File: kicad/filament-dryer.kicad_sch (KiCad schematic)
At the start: 45 parts, among them J1 Heater, J2 HEATER TEMP, J3 AREF_SELECT, J4 BOX TEMP, J5 Vdd 24V, J6 AVR-ISP-6, J7 Conn_02x07_Odd_Even, Q1 STP75NF75, Q2 2N5401, Q3 2N5551, SW1 SW_Push, U1 MIC4680-5BM, U2 ATmega8-16P, U3 LM336Z-2.5, Y1 10MHz

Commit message: schematic done, ready for pcb layout
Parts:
- removed J7: Conn_02x07_Odd_Even, Connector_PinHeader_2.54mm:PinHeader_2x02_P2.54mm_Vertical, symbol Connector_Generic:Conn_02x07_Odd_Even
- removed Q2: 2N5401, Package_TO_SOT_THT:TO-92_Inline, symbol kicad-ezee-symbols:2N5401
- removed Q3: 2N5551, Package_TO_SOT_THT:TO-92_Inline, symbol kicad-ezee-symbols:2N5551
- added CN1: Pololu Mini-LCD, Connector_PinHeader_2.54mm:PinHeader_2x07_P2.54mm_Vertical, symbol kicad-ezee-symbols:Pololu_Mini_Display
- added J7: Conn_01x06, Connector_PinHeader_2.54mm:PinHeader_1x06_P2.54mm_Vertical, symbol Connector_Generic:Conn_01x06
- added Q3: 2N3906, Package_TO_SOT_THT:TO-92_Inline, symbol Transistor_BJT:2N3906
- added Q4: 2N3904, Package_TO_SOT_THT:TO-92_Inline, symbol Transistor_BJT:2N3904
- added RV1: 10k, kicad-ezee-footprints:Potentiometer_P5.1mm_Vertical, symbol Device:R_Potentiometer_Small
- J1: footprint (none) -> kicad-ezee-footprints:TerminalBlock_2_P5.08mm
- J2, J4: footprint (none) -> Connector_PinHeader_2.54mm:PinHeader_1x02_P2.54mm_Vertical
- J3: footprint (none) -> Connector_PinHeader_2.54mm:PinHeader_2x02_P2.54mm_Vertical
- J5: value Vdd 24V -> Power
- J6: footprint (none) -> Connector_PinHeader_2.54mm:PinHeader_2x03_P2.54mm_Vertical
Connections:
- net +24V: now also C1.1, J5.1 (Pin_1), U1.2 (VIN)
- net +5V: now also C3.1, C4.1, R14.1, U2.7 (VCC), CN1.2 (Vdd), J7.1 (Pin_1), Q3.1 (E), RV1.1
- net GND: now also U1.5 (GND), U1.6 (GND), U1.7 (GND), CN1.1 (Vss), CN1.5 (R/W), J7.6 (Pin_6), Q4.1 (E), RV1.3
- net HEAT_ON: now also U2.14 (PB0)
- net Vgs: now also Q3.3 (C)
- net at R10.1, R8.2: now also Q4.2 (B)
- net at R11.2, R9.1: now also Q4.3 (C)
- net at R11.1: now also Q3.2 (B)
- net LCD_E: now reaches U2.11 (PD5)
- net LCD_E: now also CN1.6 (Enable)
- net LCD_RS: now reaches U2.12 (PD6)
- net LCD_RS: now also CN1.4 (RS)
- net PB1_OC1A: now reaches U2.15 (PB1)
- net PB1_OC1A: now also J7.5 (Pin_5)
- net RX: now reaches U2.2 (PD0)
- net RX: now also J7.2 (Pin_2)
- net LCD_DB4: now reaches U2.25 (PC2)
- net LCD_DB4: now also CN1.11 (DB4)
- net LCD_DB5: now reaches U2.26 (PC3)
- net LCD_DB5: now also CN1.12 (DB5)
- net LCD_DB6: now reaches U2.27 (PC4)
- net LCD_DB6: now also CN1.13 (DB6)
- net LCD_DB7: now reaches U2.28 (PC5)
- net LCD_DB7: now also CN1.14 (DB7)
- net TX: now reaches U2.3 (PD1)
- net TX: now also J7.3 (Pin_3)
- net PD2_INT0: now reaches U2.4 (PD2)
- net PD2_INT0: now also J7.4 (Pin_4)
- new net: CN1.3 (Vo), RV1.2
- no-connect marks 0 -> 8
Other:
- note removed: "Pololu Mini LCD pinout"
- moved on the sheet: J2, J4, R15, R17

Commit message: added fuses and fans, ready for layout
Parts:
- added F2: 5A, kicad-ezee-footprints:FuseHolder_20x5mm, symbol Device:Polyfuse
- added J8: Fresh Air Fan, Connector_PinHeader_2.54mm:PinHeader_1x02_P2.54mm_Vertical, symbol Connector_Generic:Conn_01x02
- added TH1: 10k, Resistor_THT:R_Axial_DIN0207_L6.3mm_D2.5mm_P10.16mm_Horizontal, symbol Device:Thermistor
- added TJ1: 80 deg, Connector_Wire:SolderWire-0.75sqmm_1x02_P7mm_D1.25mm_OD3.5mm, symbol Device:Thermal_Jumper
- J2: footprint Connector_PinHeader_2.54mm:PinHeader_1x02_P2.54mm_Vertical -> Connector_JST:JST_PH_B2B-PH-K_1x02_P2.00mm_Vertical
- J4: value BOX TEMP -> Circulation Fan
- J5: value Power -> 24V
- J7: value Conn_01x06 -> IO
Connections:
- net +24V: now also J4.1 (Pin_1), F2.2; no longer J5.1 (Pin_1)
- net BOX_TEMP: now also TH1.1; no longer J4.1 (Pin_1)
- net GND: now also J8.2 (Pin_2), TH1.2
- net FAN: now reaches U2.6 (PD4)
- net FAN: now also J8.1 (Pin_1)
- new net: J5.1 (Pin_1), TJ1.1 (Pin1)
- new net: F2.1, TJ1.2 (Pin2)
- no-connect marks 8 -> 7
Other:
- note added: "Runs 30 secs every 10th minute"
- note added: "Runs continously to spread heat in box"
- note added: "Tilsvarende som ovenfor, bruker mindre enn 10k resistor for å få bedre nøyaktighet rundt 50-70 grader."
- moved on the sheet: C1, C2, F1, J7, L1, U1

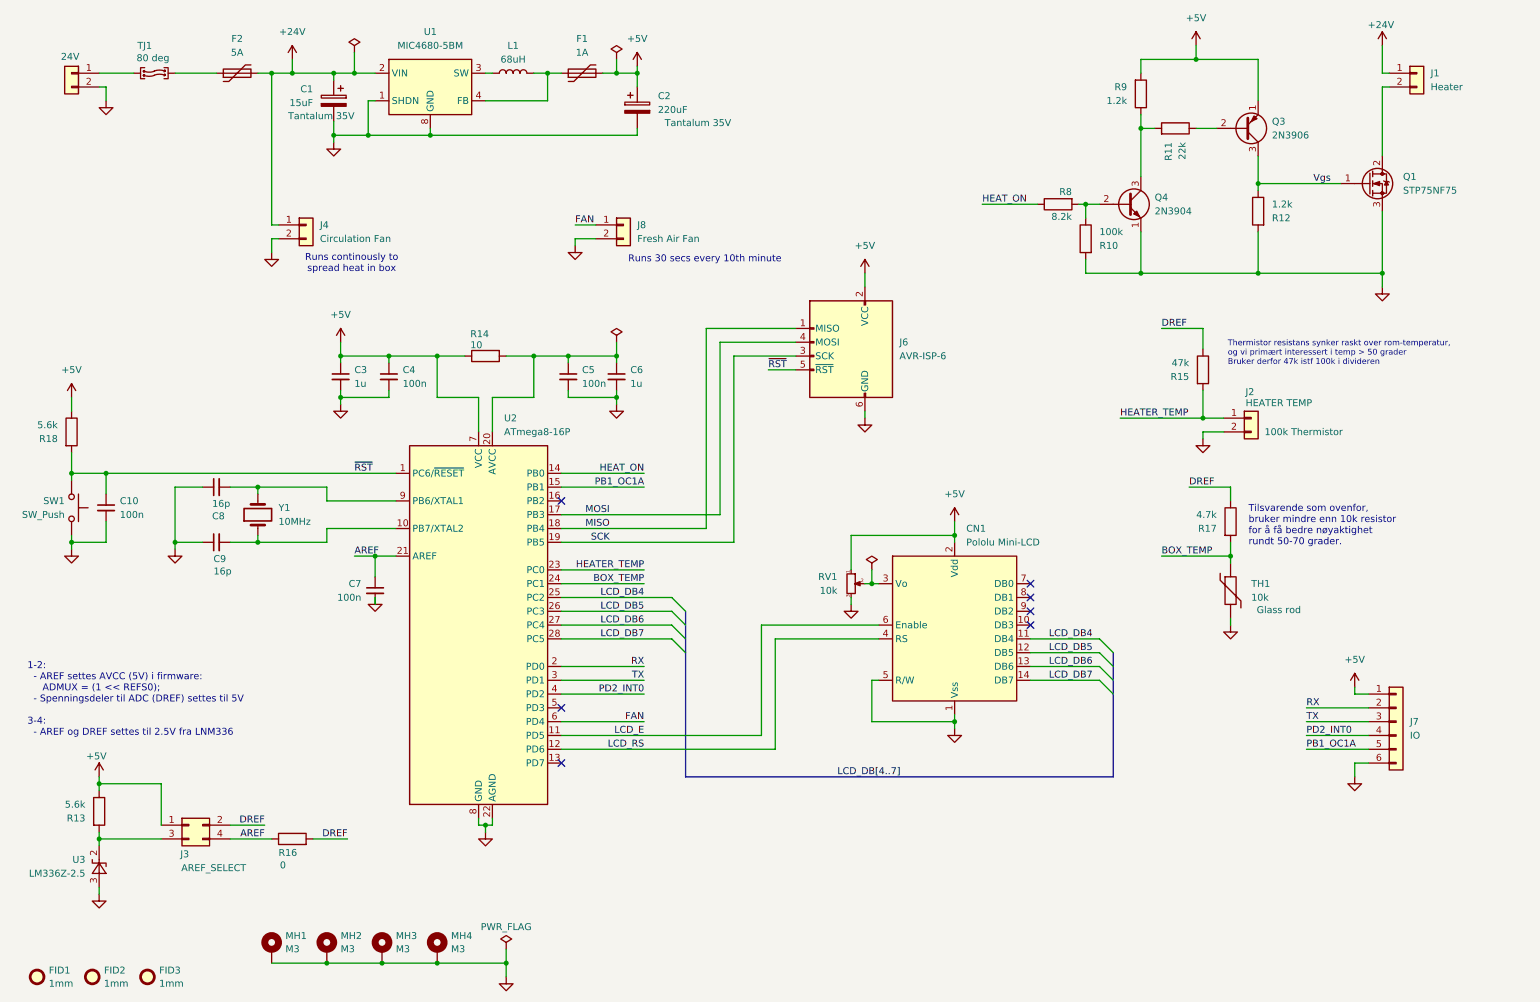
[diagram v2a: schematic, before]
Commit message: fan-control transistor, resistor values in mosfet driver
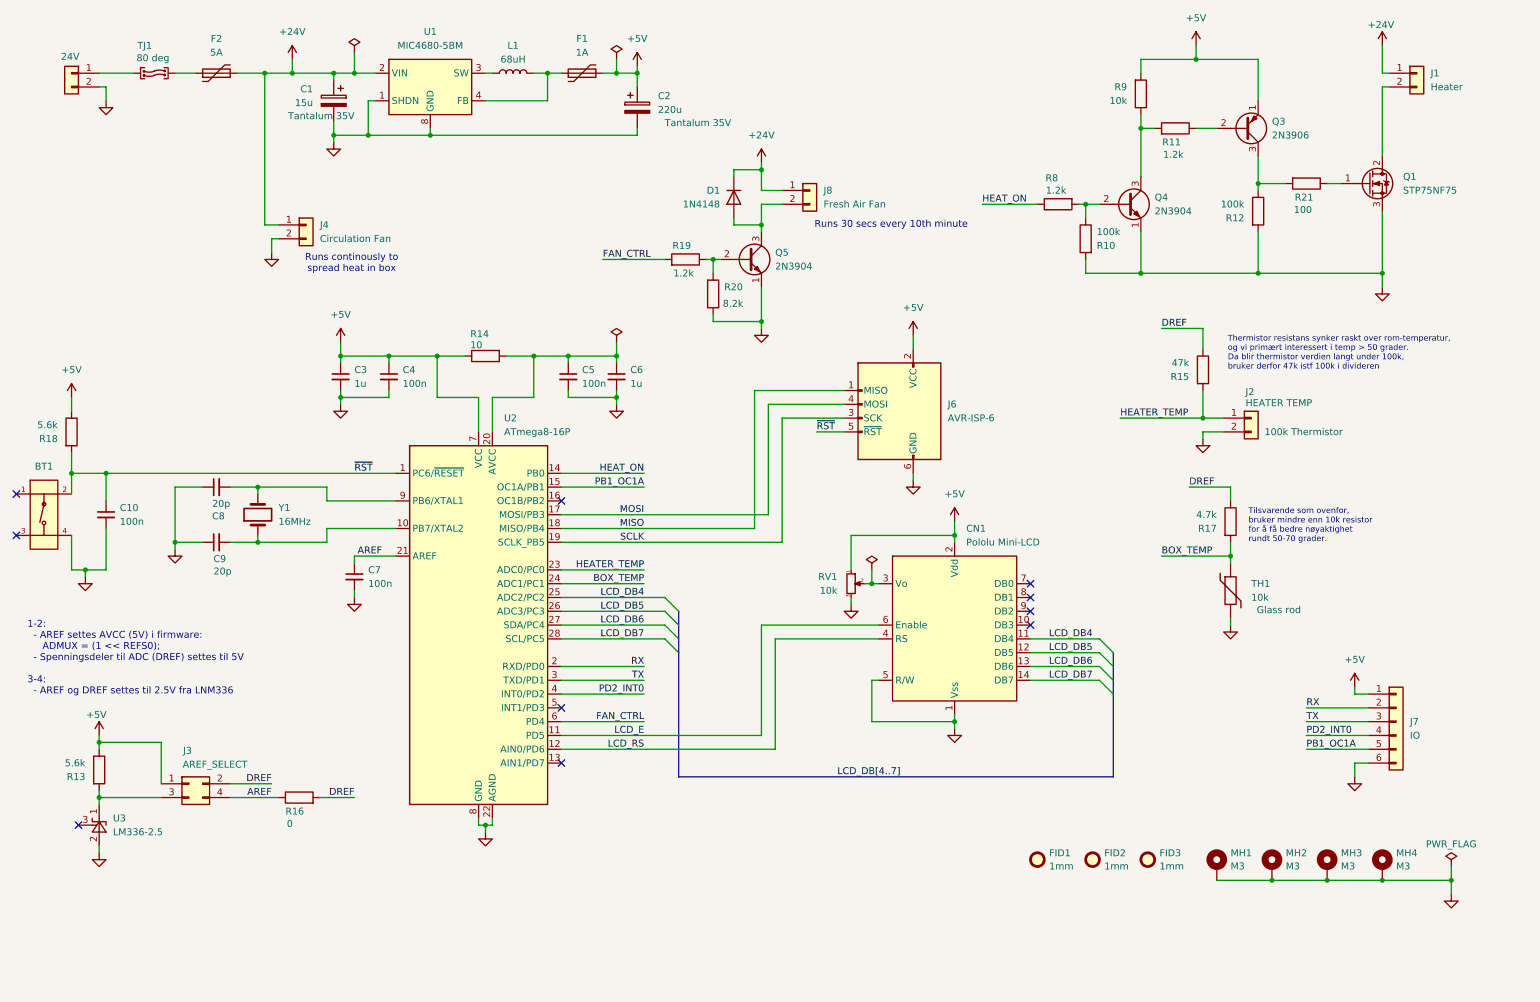
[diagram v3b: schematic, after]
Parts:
- removed SW1: SW_Push, symbol Switch:SW_Push
- removed U3: LM336Z-2.5, Package_TO_SOT_THT:TO-92_Inline, symbol kicad-ezee-symbols:LM336Z-2.5
- added BT1: Tactile Button, kicad-ezee-footprints:PushButton-SMD_4P-L5.1-W5.1, symbol kicad-ezee-symbols:Tactile_Button,_160gf,_12V,_50mA,_5.1mm
- added D1: 1N4148, Diode_THT:D_DO-35_SOD27_P7.62mm_Horizontal, symbol Diode:1N4148
- added Q5: 2N3904, Package_TO_SOT_THT:TO-92_Inline, symbol Transistor_BJT:2N3904
- added R19: 1.2k, Resistor_THT:R_Axial_DIN0207_L6.3mm_D2.5mm_P10.16mm_Horizontal, symbol Device:R
- added R20: 8.2k, Resistor_THT:R_Axial_DIN0207_L6.3mm_D2.5mm_P10.16mm_Horizontal, symbol Device:R
- added R21: 100, Resistor_THT:R_Axial_DIN0207_L6.3mm_D2.5mm_P10.16mm_Horizontal, symbol Device:R
- added U3: LM336-2.5, Package_TO_SOT_THT:TO-92L_Inline, symbol kicad-ezee-symbols:LM336-2.5
- C1: value 15uF -> 15u
- C2: value 220uF -> 220u
- C8, C9: value 16p -> 20p
- R11: value 22k -> 1.2k
- R12: value 1.2k -> 100k
- R8: value 8.2k -> 1.2k
- R9: value 1.2k -> 10k
- RV1: footprint kicad-ezee-footprints:Potentiometer_P5.1mm_Vertical -> kicad-ezee-footprints:Potentiometer_VANXY_T73YP_Vertical
- Y1: value 10MHz -> 16MHz
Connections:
- net +24V: now also J8.1 (Pin_1), D1.1 (K)
- net GND: now also BT1.4 (D), Q5.1 (E), R20.1, U3.2 (A); no longer J8.2 (Pin_2)
- net ~{RST}: now also BT1.2 (B)
- net at J3.3 (Pin_3), R13.2: now also U3.1 (K)
- net FAN renamed FAN_CTRL
- net FAN_CTRL: now also R19.2; no longer J8.1 (Pin_1)
- net SCK renamed SCLK
- net Vgs: no longer names the net of Q3.3 (C), R12.1
- net Vgs: now also R21.2; no longer Q1.1 (G)
- new net: D1.2 (A), J8.2 (Pin_2), Q5.3 (C)
- new net: Q5.2 (B), R19.1, R20.2
- new net: Q1.1 (G), R21.1
- no-connect marks 7 -> 10
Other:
- note added: "Thermistor resistans synker raskt over rom-temperatur, og vi primært interessert i temp > 50 grader. Da blir thermistor verdien langt under 100k, bruker derfor 47k istf 100k i divideren"
- note removed: "Thermistor resistans synker raskt over rom-temperatur, og vi primært interessert i temp > 50 grader Bruker derfor 47k istf 100k i divideren"
- moved on the sheet: C10, C7, F2, FID1, FID2, FID3, J3, J6, J8, MH1, MH2, MH3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

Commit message: Component placement done
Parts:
- C5: renamed from C3; footprint Capacitor_THT:C_Radial_D4.0mm_H5.0mm_P1.50mm -> Capacitor_Tantalum_SMD:CP_EIA-6032-20_AVX-F
- C9: renamed from C6; footprint Capacitor_THT:C_Radial_D4.0mm_H5.0mm_P1.50mm -> Capacitor_Tantalum_SMD:CP_EIA-6032-20_AVX-F
- renumbered C10 to C1, C2 to C10, C8 to C2, C9 to C3, C1 to C4, C7 to C6, C4 to C7, C5 to C8, F2 to F1, F1 to F2, J5 to J1, J3 to J2, J4 to J3, J8 to J4, J6 to J5, J2 to J6, J1 to J8, Q5 to Q1, Q4 to Q2, Q1 to Q4, R18 to R1, R11 to R10, R15 to R11, R17 to R12, R12 to R13, R21 to R14, R13 to R2, R16 to R3, R14 to R4, R19 to R5, R20 to R6, R8 to R7, R10 to R8, U2 to U1, U1 to U2
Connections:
- net +5V: no longer C10.1
- net at F2.1, L1.2, U2.4 (FB): now also C10.1
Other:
- moved on the sheet: C10, C9, F2

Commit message: Created buck with MC34063 for 13.2v
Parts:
- removed J3: Circulation Fan, Connector_PinHeader_2.54mm:PinHeader_1x02_P2.54mm_Vertical, symbol Connector_Generic:Conn_01x02
- added C11: 100u, Capacitor_Tantalum_SMD:CP_EIA-6032-28_Kemet-C, symbol Device:C_Polarized
- added C12, C14, C15: 100n, Capacitor_THT:C_Disc_D4.3mm_W1.9mm_P5.00mm, symbol Device:C_Small
- added C13: 680u, symbol Device:C_Polarized
- added D2, D3: 1N4004, Diode_THT:D_DO-41_SOD81_P10.16mm_Horizontal, symbol Diode:1N4004
- added D4: 1N5822, Diode_THT:D_DO-201AD_P15.24mm_Horizontal, symbol Diode:1N5822
- added J9: Conn_01x04, symbol Connector_Generic:Conn_01x04
- added L2: 220uH, Inductor_SMD:L_12x12mm_H6mm, symbol Device:L
- added Q5: 2N3906, Package_TO_SOT_THT:TO-92_Inline, symbol Transistor_BJT:2N3906
- added R15: 47, Resistor_THT:R_Axial_DIN0207_L6.3mm_D2.5mm_P10.16mm_Horizontal, symbol Device:R
- added R16: 0.3, 1/2w, Resistor_THT:R_Axial_DIN0207_L6.3mm_D2.5mm_P10.16mm_Horizontal, symbol Device:R
- added R17: 11.7k, Resistor_THT:R_Axial_DIN0207_L6.3mm_D2.5mm_P10.16mm_Horizontal, symbol Device:R
- added R18: 1.21k, Resistor_THT:R_Axial_DIN0207_L6.3mm_D2.5mm_P10.16mm_Horizontal, symbol Device:R
- added R19: 2.2k, Resistor_THT:R_Axial_DIN0207_L6.3mm_D2.5mm_P10.16mm_Horizontal, symbol Device:R
- added R20: 4.7k, Resistor_THT:R_Axial_DIN0207_L6.3mm_D2.5mm_P10.16mm_Horizontal, symbol Device:R
- added U4: MC34063AP, Package_DIP:DIP-8_W7.62mm, symbol Regulator_Switching:MC34063AP
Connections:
- net +24V: now also C11.1, C12.1, R16.1, U4.6 (Vin), U4.8 (DC)
- net GND: now also C11.2, C12.2, C13.2, C14.2, C15.2, D4.2 (A), J9.1 (Pin_1), R18.2, U4.4 (GND)
- new net: C15.1, Q5.3 (C), R20.2
- new net: D4.1 (K), L2.1, U4.2 (SwE)
- new net: D3.1 (K), J9.2 (Pin_2), R15.2, R19.2
- new net: D2.1 (K), D3.2 (A)
- new net: R17.2, R18.1, U4.5 (Vfb)
- new net: Q5.2 (B), R19.1
- new net: R16.2, U4.1 (SwC), U4.7 (Ipk)
- new net +13.2V: C13.1, C14.1, D2.2 (A), L2.2, Q5.1 (E), R15.1, R17.1
- new net PWM: J9.4 (Pin_4)
- new net Tach: J9.3 (Pin_3)
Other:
- note added: "I(R15)=1.2/47=26mA"
- note removed: "Runs continously to spread heat in box"
- moved on the sheet: C10, C4, D1, F1, F2, J2, J4, L1, Q1, R2, R3, R5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
